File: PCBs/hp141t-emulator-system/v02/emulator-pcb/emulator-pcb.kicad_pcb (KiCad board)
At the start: 2 copper layers, 136.3 x 86.1 mm, 53 parts, among them J1 Conn_Coaxial, J2 Conn_Coaxial, J3 Conn_Coaxial, J4 Mini-DIN-5, Q1 2N2222, U1 LM358, U2 XR2206CP, U3 XR2206CP

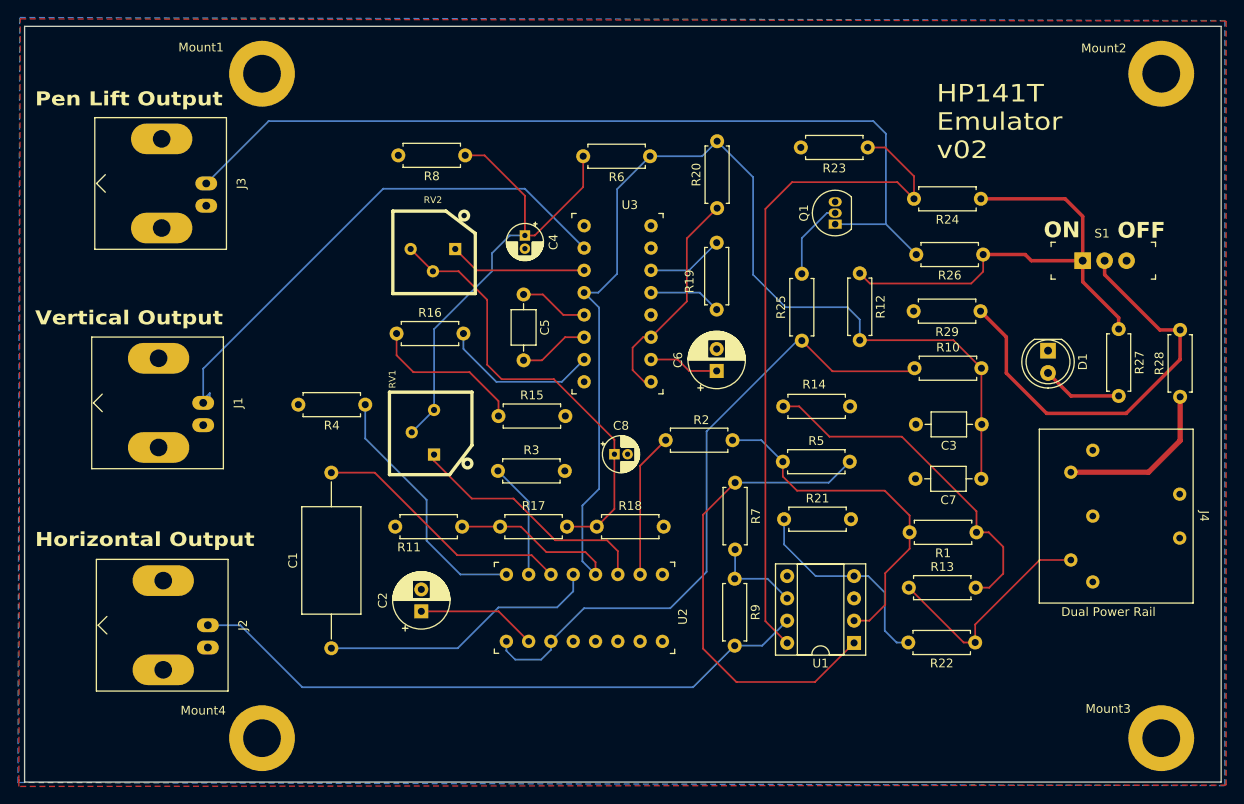
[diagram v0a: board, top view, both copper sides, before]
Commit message: Removed voltage divider. Added 0.1uF power capacitors.
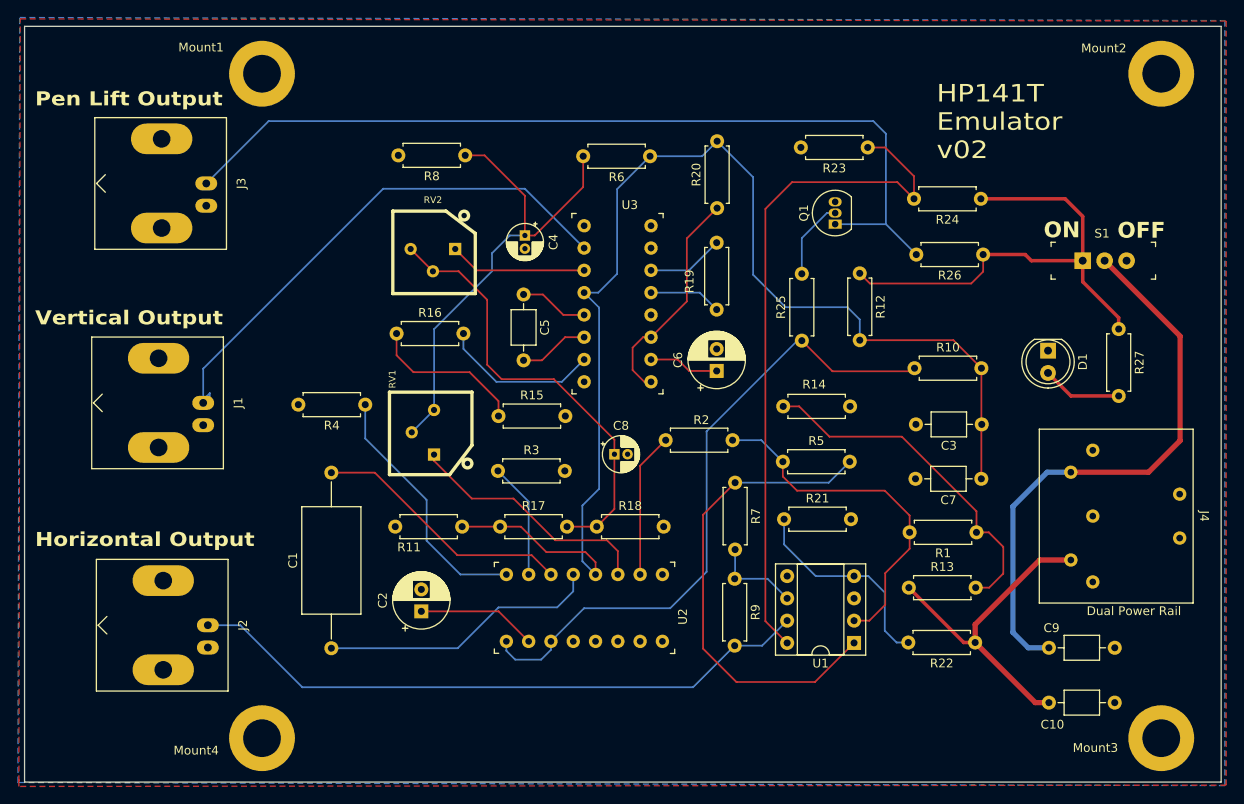
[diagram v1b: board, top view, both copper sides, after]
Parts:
- removed R28: 33k, Resistor_THT:R_Axial_DIN0207_L6.3mm_D2.5mm_P7.62mm_Horizontal
- removed R29: 10k, Resistor_THT:R_Axial_DIN0207_L6.3mm_D2.5mm_P7.62mm_Horizontal
- added C10: 0.1uF, Capacitor_THT:C_Axial_L3.8mm_D2.6mm_P7.50mm_Horizontal, F.Cu at (195.2, 140.8)
- added C9: 0.1uF, Capacitor_THT:C_Axial_L3.8mm_D2.6mm_P7.50mm_Horizontal, F.Cu at (187.7, 134.5)
- R27: value 100k -> 2.2k
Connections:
- J4 pad 4: Net-(J4-Pad4) -> Net-(C9-Pad1)
- S1 pad 2: Net-(R28-Pad2) -> Net-(C9-Pad1)
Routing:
- net Net-(C9-Pad1): track 0.00 -> 65.4 mm
- net Net-(R28-Pad2): track 48.7 -> 0.00 mm
- net Net-(J4-Pad4): track 18.9 -> 0.00 mm
- net -12V: track 26.1 -> 37.4 mm
